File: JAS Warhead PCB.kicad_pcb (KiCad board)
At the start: 2 copper layers, 92 x 89.9 mm, 90 parts, among them J1 Conn_01x02_Socket, J10 Conn_01x02_Socket, J11 Conn_01x02_Socket, J12 Conn_01x02_Pin, J13 Conn_01x02_Pin, J14 Conn_01x02_Pin, J2 Conn_01x02_Socket, J3 Conn_01x02_Socket, J4 Conn_01x02_Socket, J5 Conn_01x02_Socket, J6 Conn_01x02_Socket, J7 Conn_01x02_Socket, J8 Conn_01x15_Socket, J9 Conn_01x15_Socket, K1 Panasonic_ALFG1PF12, K2 Panasonic_ALFG1PF12, Q1 PN2222A, Q2 PN2222A, U10 AP2127R-3.3, U2 AP2127R-3.3, U3 AP2127R-3.3, U4 LD1117S50TR_SOT223, U5 MAX31855KASA, U6 MAX31855KASA, U7 MAX31855KASA, U8 AP2127R-3.3, U9 MAX31855KASA

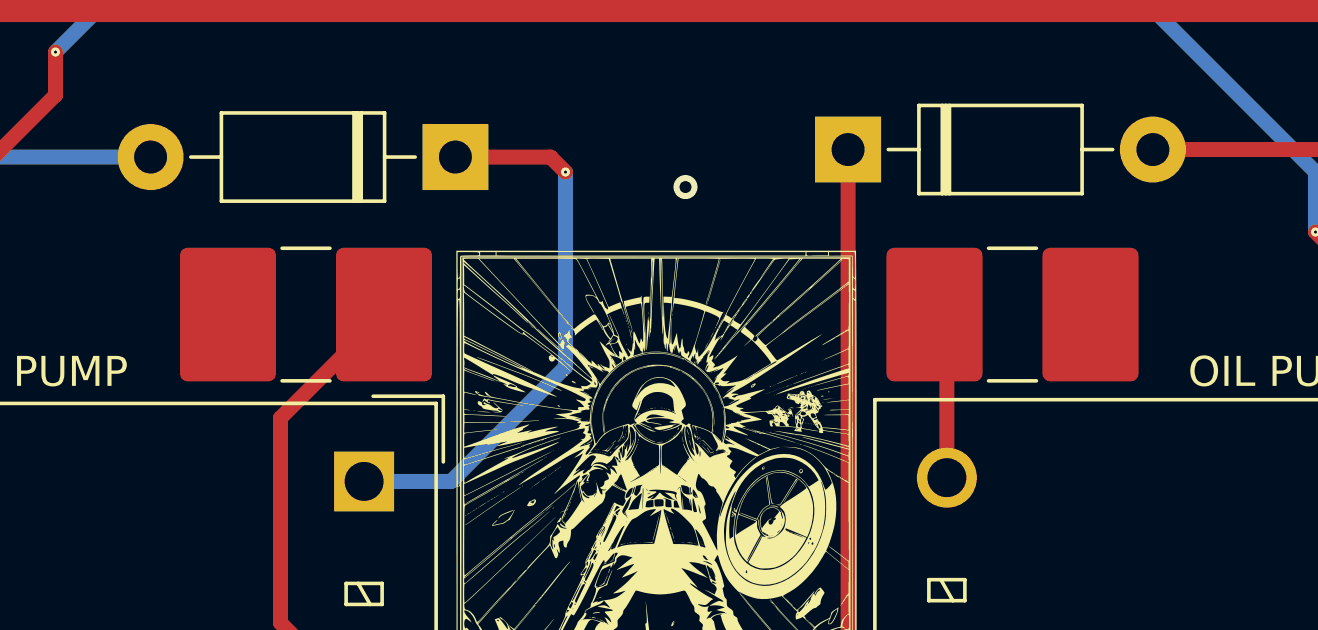
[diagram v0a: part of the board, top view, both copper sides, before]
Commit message: remove handsolder
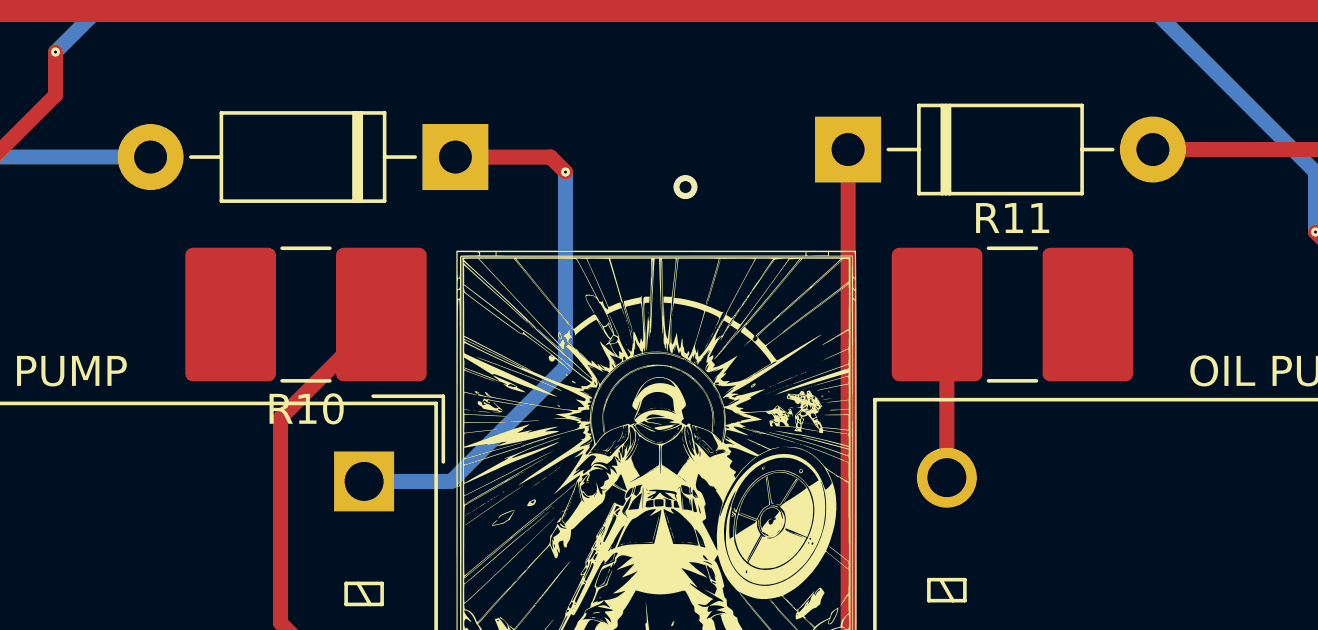
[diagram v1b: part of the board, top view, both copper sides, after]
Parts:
- R10, R11: footprint Resistor_SMD:R_2816_7142Metric_Pad3.20x4.45mm_HandSolder -> Resistor_SMD:R_2816_7142Metric
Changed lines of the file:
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@@
 		)
 	)
-	(footprint "Resistor_SMD:R_2816_7142Metric_Pad3.20x4.45mm_HandSolder"
+	(footprint "Resistor_SMD:R_2816_7142Metric"
 		(layer "F.Cu")
 		(at 147.9 123.75)
-		(descr "Resistor SMD 2816 (7142 Metric), square (rectangular) end terminal, IPC_7351 nominal with elongated pad for handsoldering. (Body size from: https://www.vishay.com/docs/30100/wsl.pdf), generated with kicad-footprint-generator")
-		(tags "resistor handsolder")
+		(descr "Resistor SMD 2816 (7142 Metric), square (rectangular) end terminal, IPC_7351 nominal, (Body size from: https://www.vishay.com/docs/30100/wsl.pdf), generated with kicad-footprint-generator")
+		(tags "resistor")
 		(property "Reference" "R11"
 			(at 0 -3.18 0)
 			(layer "F.SilkS")
-			(hide yes)
 			(effects
 				(font
@@
 			(at 0 3.18 0)
 			(layer "F.Fab")
-			(hide yes)
 			(effects
 				(font
@@
 			)
 		)
-		(property "Footprint" "Resistor_SMD:R_2816_7142Metric_Pad3.20x4.45mm_HandSolder"
+		(property "Footprint" "Resistor_SMD:R_2816_7142Metric"
 			(at 0 0 0)
 			(unlocked yes)
@@
 		)
 		(fp_line
-			(start -4.45 -2.48)
-			(end 4.45 -2.48)
+			(start -4.28 -2.48)
+			(end 4.28 -2.48)
 			(stroke
 				(width 0.05)
@@
 		)
 		(fp_line
-			(start -4.45 2.48)
-			(end -4.45 -2.48)
+			(start -4.28 2.48)
+			(end -4.28 -2.48)
 			(stroke
 				(width 0.05)
@@
 		)
 		(fp_line
-			(start 4.45 -2.48)
-			(end 4.45 2.48)
+			(start 4.28 -2.48)
+			(end 4.28 2.48)
 			(stroke
 				(width 0.05)
@@
 		)
 		(fp_line
-			(start 4.45 2.48)
-			(end -4.45 2.48)
+			(start 4.28 2.48)
+			(end -4.28 2.48)
 			(stroke
 				(width 0.05)
@@
 		)
 		(pad "1" smd roundrect
-			(at -2.6 0)
-			(size 3.2 4.45)
+			(at -2.5125 0)
+			(size 3.025 4.45)
 			(layers "F.Cu" "F.Paste" "F.Mask")
-			(roundrect_rratio 0.078125)
+			(roundrect_rratio 0.082645)
 			(net 59 "Net-(K2-PadA2)")
 			(pintype "passive")
 		)
 		(pad "2" smd roundrect
-			(at 2.6 0)
-			(size 3.2 4.45)
+			(at 2.5125 0)
+			(size 3.025 4.45)
 			(layers "F.Cu" "F.Paste" "F.Mask")
-			(roundrect_rratio 0.078125)
+			(roundrect_rratio 0.082645)
 			(net 1 "GND")
 			(pintype "passive")
@@
 		)
 	)
-	(footprint "Resistor_SMD:R_2816_7142Metric_Pad3.20x4.45mm_HandSolder"
+	(footprint "Resistor_SMD:R_2816_7142Metric"
 		(layer "F.Cu")
 		(at 124.35 123.75 180)
-		(descr "Resistor SMD 2816 (7142 Metric), square (rectangular) end terminal, IPC_7351 nominal with elongated pad for handsoldering. (Body size from: https://www.vishay.com/docs/30100/wsl.pdf), generated with kicad-footprint-generator")
-		(tags "resistor handsolder")
+		(descr "Resistor SMD 2816 (7142 Metric), square (rectangular) end terminal, IPC_7351 nominal, (Body size from: https://www.vishay.com/docs/30100/wsl.pdf), generated with kicad-footprint-generator")
+		(tags "resistor")
 		(property "Reference" "R10"
 			(at 0 -3.18 180)
 			(layer "F.SilkS")
-			(hide yes)
 			(effects
 				(font
@@
 			(at 0 3.18 180)
 			(layer "F.Fab")
-			(hide yes)
 			(effects
 				(font
@@
 			)
 		)
-		(property "Footprint" "Resistor_SMD:R_2816_7142Metric_Pad3.20x4.45mm_HandSolder"
+		(property "Footprint" "Resistor_SMD:R_2816_7142Metric"
 			(at 0 0 180)
 			(unlocked yes)
@@
 		)
 		(fp_line
-			(start 4.45 2.48)
-			(end -4.45 2.48)
+			(start 4.28 2.48)
+			(end -4.28 2.48)
 			(stroke
 				(width 0.05)
@@
 		)
 		(fp_line
-			(start 4.45 -2.48)
-			(end 4.45 2.48)
+			(start 4.28 -2.48)
+			(end 4.28 2.48)
 			(stroke
 				(width 0.05)
@@
 		)
 		(fp_line
-			(start -4.45 2.48)
-			(end -4.45 -2.48)
+			(start -4.28 2.48)
+			(end -4.28 -2.48)
 			(stroke
 				(width 0.05)
@@
 		)
 		(fp_line
-			(start -4.45 -2.48)
-			(end 4.45 -2.48)
+			(start -4.28 -2.48)
+			(end 4.28 -2.48)
 			(stroke
 				(width 0.05)
@@
 		)
 		(pad "1" smd roundrect
-			(at -2.6 0 180)
-			(size 3.2 4.45)
+			(at -2.5125 0 180)
+			(size 3.025 4.45)
 			(layers "F.Cu" "F.Paste" "F.Mask")
-			(roundrect_rratio 0.078125)
+			(roundrect_rratio 0.082645)
 			(net 58 "Net-(K1-PadA2)")
 			(pintype "passive")
 		)
 		(pad "2" smd roundrect
-			(at 2.6 0 180)
-			(size 3.2 4.45)
+			(at 2.5125 0 180)
+			(size 3.025 4.45)
 			(layers "F.Cu" "F.Paste" "F.Mask")
-			(roundrect_rratio 0.078125)
+			(roundrect_rratio 0.082645)
 			(net 1 "GND")
 			(pintype "passive")

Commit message: update positioning
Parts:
- moved J14 9.50 mm to (93.0, 65.5)
- moved G*** 5.62 mm to (98.0, 77.5), turned to -135 degrees
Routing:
- net /3V3: track 37.4 -> 46.9 mm

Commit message: start compliance with PCBway
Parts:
- J1, J10, J11, J2, J7: footprint TerminalBlock_4Ucon:TerminalBlock_4Ucon_1x02_P3.50mm_Vertical -> TerminalBlock:TerminalBlock_bornier-2_P5.08mm
- J3, J4, J5, J6: footprint TerminalBlock_4Ucon:TerminalBlock_4Ucon_1x02_P3.50mm_Horizontal -> TerminalBlock:TerminalBlock_bornier-2_P5.08mm
- moved C2 8.85 mm to (158.0, 101.8)
- moved U4 6.76 mm to (161.3, 106.5)
- moved C1 3.29 mm to (177.2, 100.2)
- moved J1 2.91 mm to (177.2, 136.6), turned to 90 degrees
- moved J2 2.84 mm to (94.2, 131.8), turned to -90 degrees
- moved J7 1.77 mm to (177.2, 109.3)
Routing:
- net +5V: track 169.8 -> 159.5 mm
- net Net-(J1-Pin_2): track 25.0 -> 19.6 mm, vias 0 -> 1
- net GND: track 11.6 -> 16.1 mm, vias 6 -> 7
- net +12V: track 127.6 -> 131.0 mm
- net /CS4: track 17.6 -> 18.6 mm
- net Net-(J2-Pin_2): track 20.8 -> 21.2 mm, vias 0 -> 1

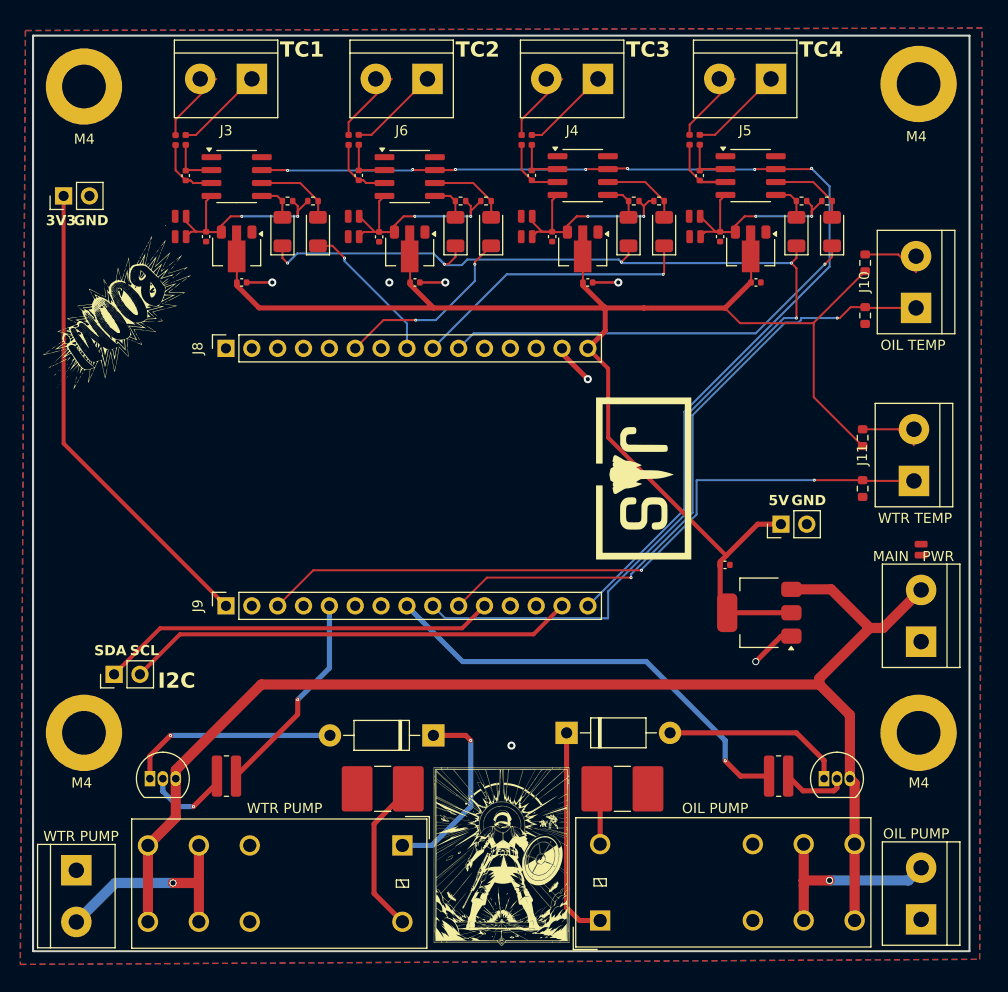
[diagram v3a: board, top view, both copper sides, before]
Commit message: edits to conform to design regulation
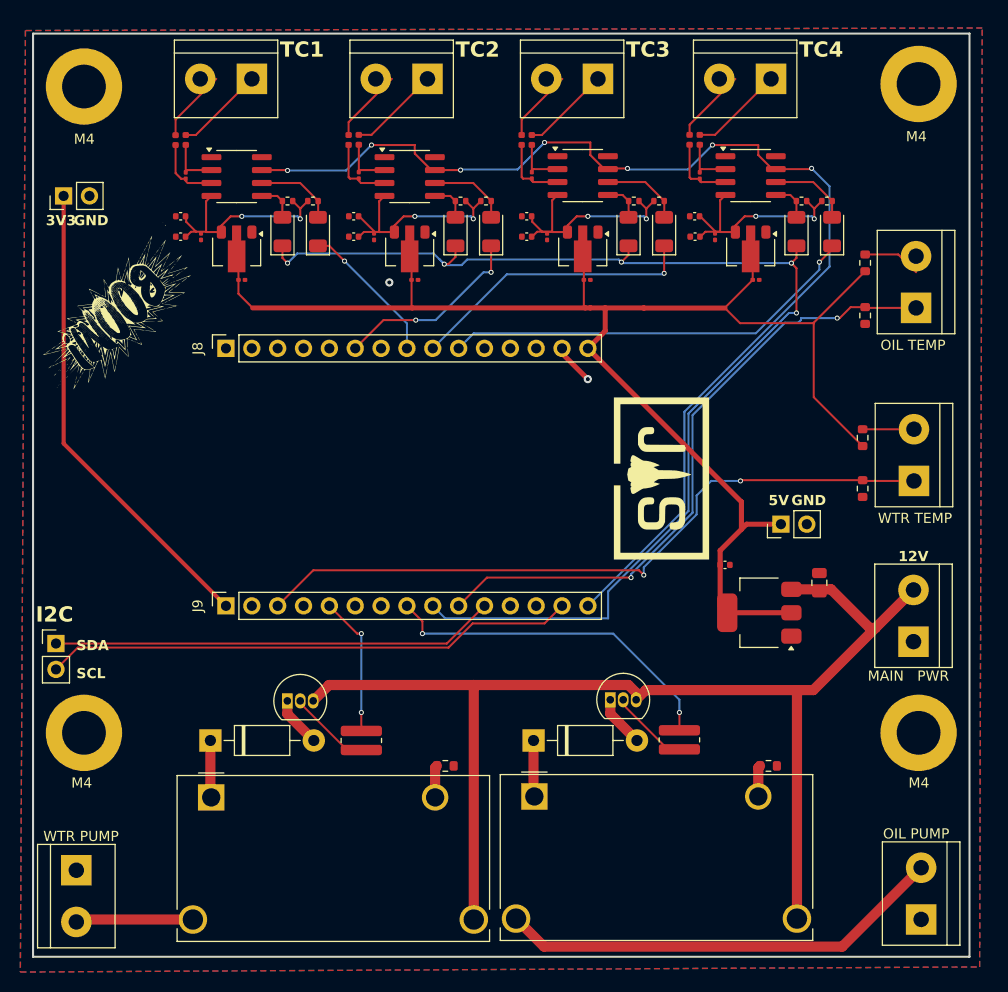
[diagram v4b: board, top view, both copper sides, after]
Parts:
- removed the G*** at (136.0, 130.2)
- removed K1, K2: Panasonic_ALFG1PF12, Relay_THT:Relay_SPDT_Omron_G2RL-1-E
- added K3: Panasonic_ALFG1PF12, Relay_THT:Relay_SPST_Panasonic_ALFG_FormA_CircularHoles, F.Cu at (139.2, 124.5)
- added K4: Panasonic_ALFG1PF12, Relay_THT:Relay_SPST_Panasonic_ALFG_FormA_CircularHoles, F.Cu at (107.5, 124.6)
- C1: value 3.3uF -> 10uF; footprint Capacitor_SMD:C_0504_1310Metric -> Capacitor_SMD:C_0805_2012Metric
- C10, C13, C14, C15, C18, C19, C20, C23, C3, C4, C5, C9: footprint Capacitor_SMD:C_0402_1005Metric -> Capacitor_SMD:C_0201_0603Metric
- C11, C12, C16, C17, C21, C22, C6, C7: footprint Capacitor_SMD:C_0504_1310Metric -> Capacitor_SMD:C_0402_1005Metric
- C2: value 0.2uF -> 10uF
- R10, R11: footprint Resistor_SMD:R_2816_7142Metric -> Resistor_SMD:R_0603_1608Metric
- moved Q1 22.4 mm to (146.7, 115.0)
- moved D1 21.9 mm to (107.4, 119.0), turned to 0 degrees
- moved Q2 15.5 mm to (115.0, 115.1)
- moved R11 14.5 mm to (162.2, 121.5)
- moved R1 13.7 mm to (122.2, 119.0), turned to 90 degrees
- moved C1 10.5 mm to (167.2, 103.5)
- moved R12 10.4 mm to (153.5, 118.9), turned to 90 degrees
- moved R10 6.55 mm to (130.5, 121.5), turned to 0 degrees
- moved J12 6.46 mm to (92.2, 109.5), turned to 0 degrees
- moved D10 3.34 mm to (139.2, 119.0)
- moved G*** 1.75 mm to (151.8, 93.2)
- moved J7 0.75 mm to (176.5, 109.3)
- moved C20 0.50 mm to (123.5, 69.5)
- moved C10 0.50 mm to (140.5, 69.5)
- moved C15 0.50 mm to (157.0, 69.5)
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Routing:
- net Net-(J1-Pin_2): track 19.6 -> 44.1 mm, vias 1 -> 0
- net Net-(D1-A): track 20.8 -> 4.97 mm, vias 1 -> 0
- net Net-(D10-K): track 21.0 -> 5.53 mm
- net Net-(D1-K): track 18.7 -> 5.63 mm, vias 1 -> 0
- net Net-(D10-A): track 18.0 -> 5.09 mm
- net Net-(K4-PadA2): track 15.6 -> 3.16 mm
- net GND: track 16.1 -> 4.07 mm, vias 7 -> 2
- net +12V: track 131.0 -> 120.6 mm
- net Net-(J2-Pin_2): track 21.2 -> 11.5 mm, vias 1 -> 0
- net /RELAY2: track 43.7 -> 34.3 mm, vias 1 -> 2
- net /SCL: track 43.8 -> 52.3 mm
- net /SPI Data_In: track 107.9 -> 115.7 mm
- net /RELAY1: track 20.5 -> 13.8 mm, vias 1 -> 2
- net /SDA: track 39.2 -> 43.6 mm
- net +5V: track 159.5 -> 156.8 mm
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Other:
- board size 92 x 89.9 mm -> 92 x 90.7 mm
- board text added: "12V"

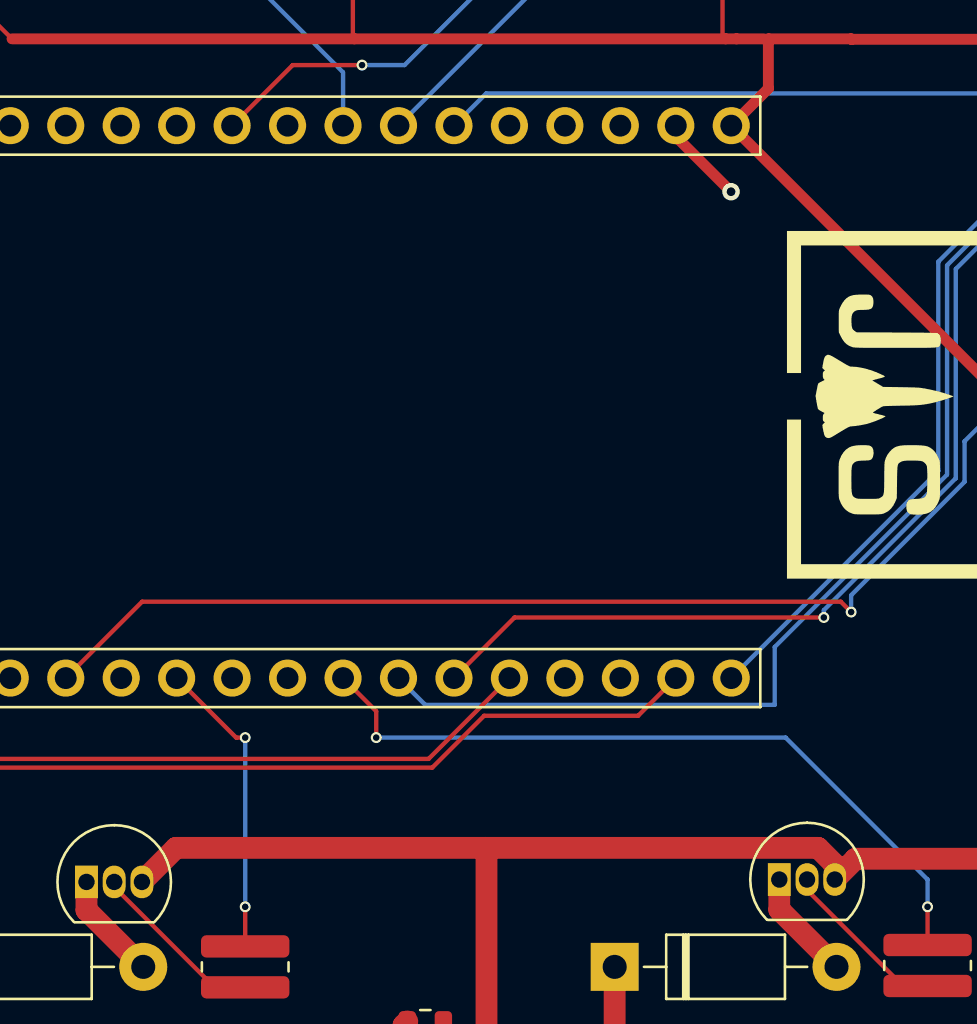
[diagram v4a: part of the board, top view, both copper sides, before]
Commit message: move some traces
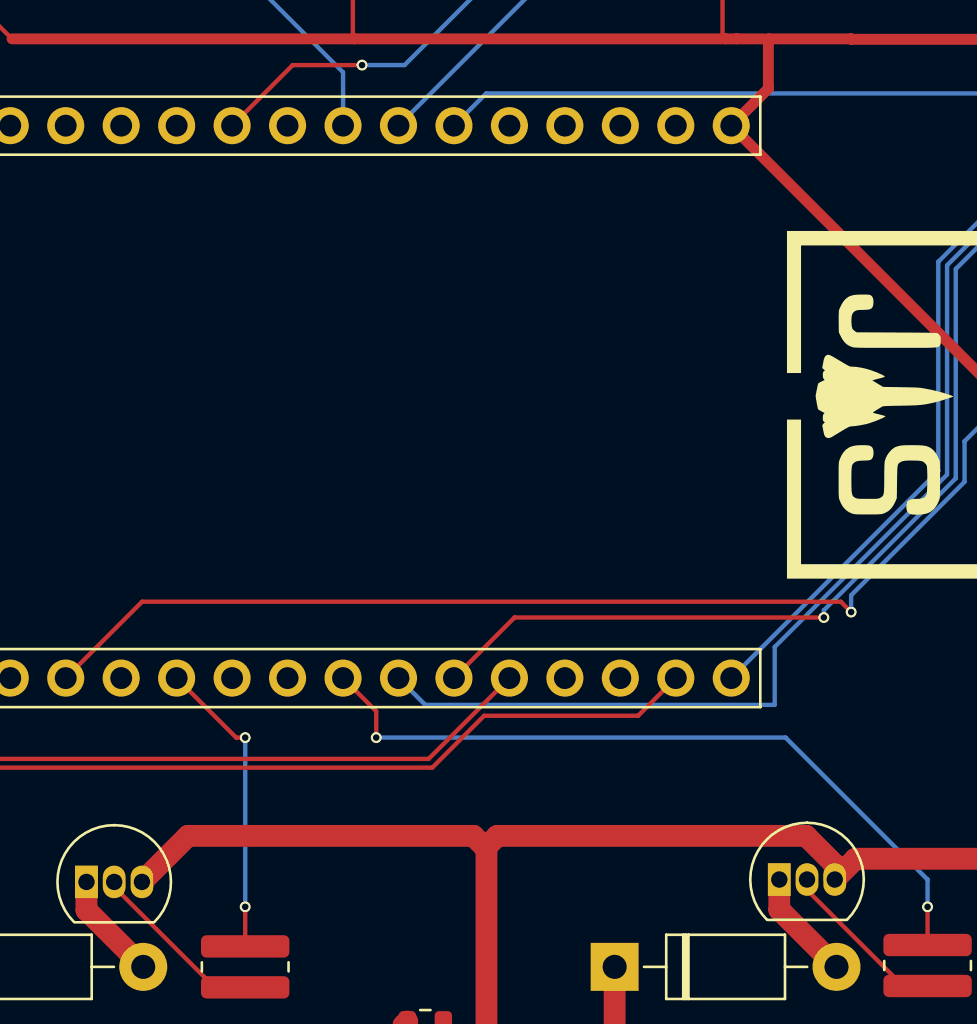
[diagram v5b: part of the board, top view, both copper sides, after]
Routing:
- net GND: track 4.07 -> 0.50 mm, vias 2 -> 1
- net +12V: track 120.6 -> 121.5 mm
